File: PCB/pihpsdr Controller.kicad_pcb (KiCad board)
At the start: 2 copper layers, 243 x 154 mm, 167 parts, among them IC1 MCP23017T-E_SO, IC2 MCP23017T-E_SO, IC3 M24C32-RDW6TP, IC4 74LV1T125GVH, IC5 74LV1T125GVH, IC6 WM8960CGEFL_V, IC7 DS3231MZ_V+, IC8 Pico, J1 615008143721, J2 1725672, J3 485-1992, J4 SJ-3566AN, J5 SJ-3523-SMT-TR, J6 10129379-905001BLF, J7 Conn_01x02, J8 PJ-102AH, J9 MJ-3523-SMT, Q1 FDD6685, Q2 2N7002K, SW0 B3F-1055, SW1 B3F-1055, SW10 B3F-1055, SW11 B3F-1055, SW12 B3F-1055, SW13 B3F-1055, SW14 B3F-1055, SW15 B3F-1055, SW16 B3F-1055, SW2 B3F-1055, SW3 B3F-1055, SW4 B3F-1055, SW5 B3F-1055, SW6 B3F-1055, SW7 B3F-1055, SW8 B3F-1055, SW9 B3F-1055, U1 LMZ22005TZ_NOPB, U2 BAT-HLD-001, Y1 TSX-3225_24.0000MF18X-C

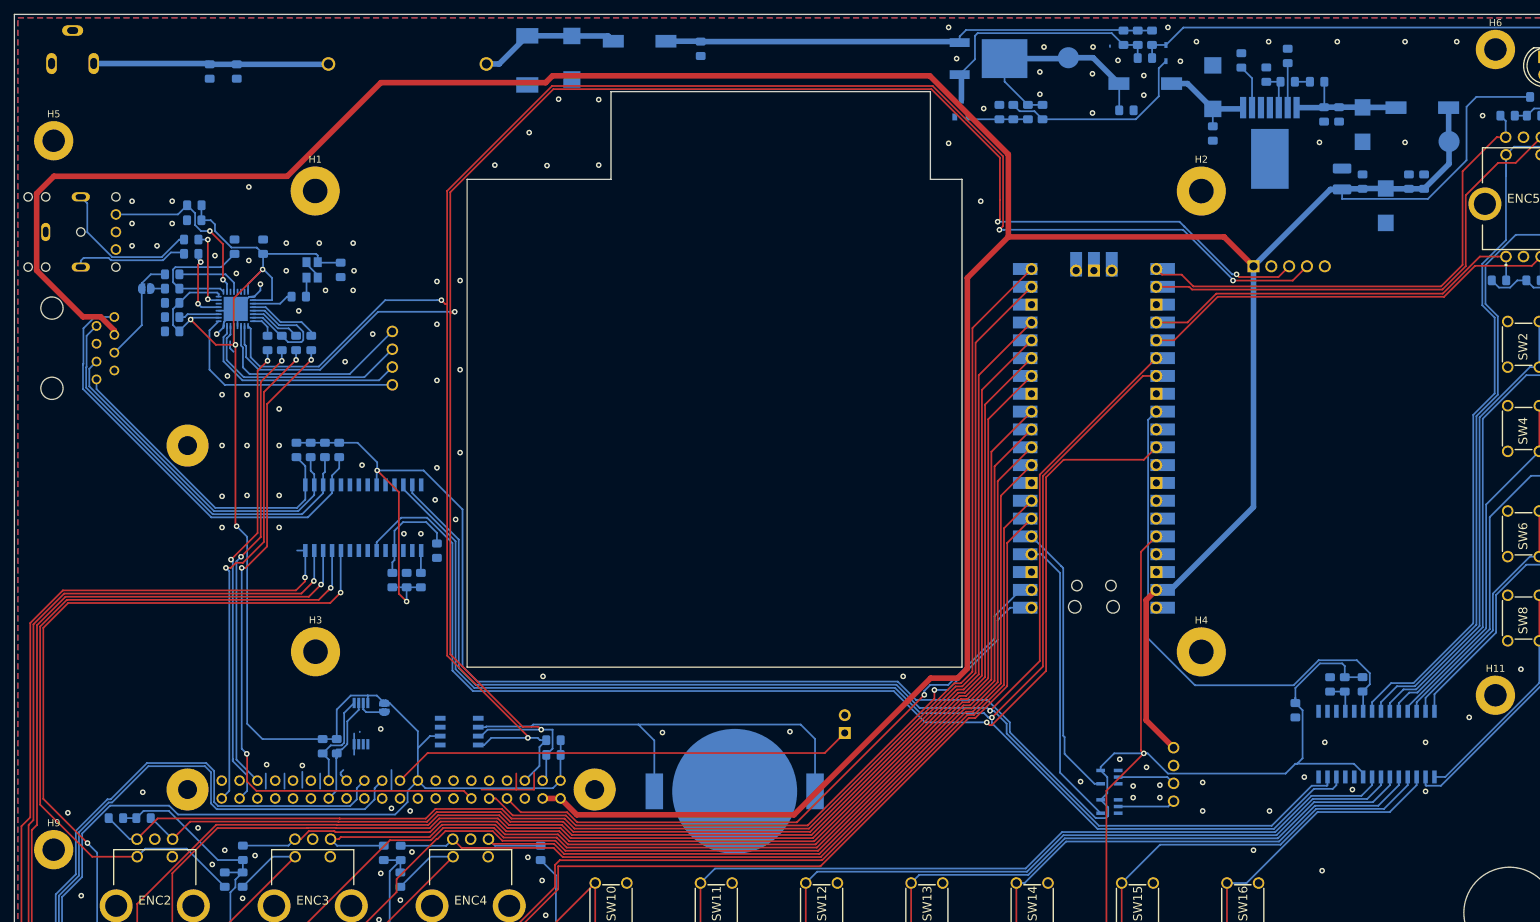
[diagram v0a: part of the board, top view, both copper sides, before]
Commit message: Completed parts details on schematics and recreated gerbers and bom.
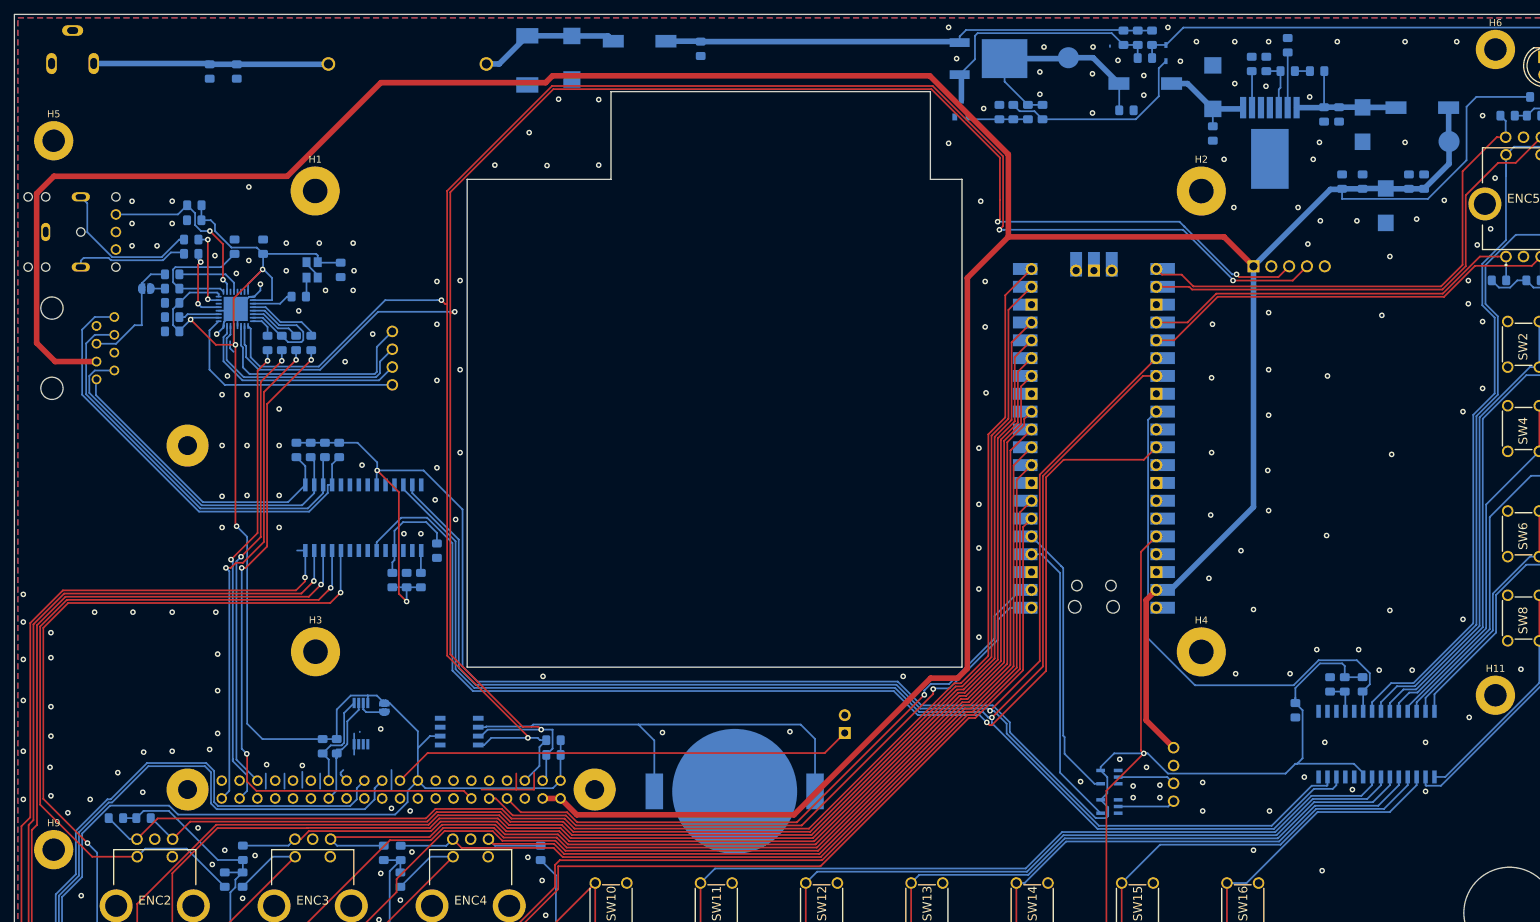
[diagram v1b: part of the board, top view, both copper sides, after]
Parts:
- C10, C11, C4, C9: value 4,7uF -> 4,7uF / 16V
- C12, C21, C23, C25: value 100nF 35V -> 0,1uF / 50V
- C13: value 0,1uF -> 0,1uF / 50V
- C14: value 10uF/35V -> 10uF / 35V
- C17: value 1uF / 10V -> 1uF / 50V
- C19: value 100nF -> 0,1uF / 50V
- C2: value 1µ -> 1uF / 50V
- C20, C24: value 10uF 35V -> 10uF / 35V
- C26: value 0,47nF -> 0,47uF / 16V
- C27, C30: value 100nF / 10V -> 0,1uF / 50V
- C33: value 10u -> 10u / 35V
- C34: value 100uF / 6.3V -> 100uF / 10V; footprint Capacitor_SMD:C_1210_3225Metric_Pad1.42x2.65mm_HandSolder -> Capacitor_SMD:C_0805_2012Metric_Pad1.15x1.40mm_HandSolder
- C5: value 0,1µF -> 0,1uF / 50V
- C6: value 0,1u -> 0,1uF / 50V
- C7, C8: value 100µF 10V -> 100uF / 10V
- moved R59 1.56 mm to (201.3, 22.1)
- moved C26 1.52 mm to (206.4, 19.4)
- moved R60 1.52 mm to (203.4, 22.1)
- moved R61 1.52 mm to (206.4, 23.1)
- moved R62 1.52 mm to (210.6, 23.1)
- moved C34 0.38 mm to (214.2, 38.8)
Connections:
- IC2 pad 1: MIC_FAST_SCAN -> MIC_BTN_DOWN
- IC2 pad 2: MIC_PTT -> MIC_BTN_UP
- IC2 pad 3: MIC_BTN_UP -> MIC_PTT
- IC2 pad 4: MIC_BTN_DOWN -> MIC_FAST_SCAN
- J1 pad 1: MIC_FAST_SCAN -> MIC_BTN_DOWN
- J1 pad 2: GND -> MIC_BTN_UP
- J1 pad 3: MIC_PTT -> +5V
- J1 pad 4: MIC+ -> GND
- J1 pad 5: GND -> MIC+
- J1 pad 6: +5V -> MIC_PTT
- J1 pad 7: MIC_BTN_UP -> GND
- J1 pad 8: MIC_BTN_DOWN -> MIC_FAST_SCAN
- R45 pad 2: MIC_FAST_SCAN -> MIC_BTN_DOWN
- R46 pad 2: MIC_PTT -> MIC_BTN_UP
- R47 pad 2: MIC_BTN_UP -> MIC_PTT
- R48 pad 2: MIC_BTN_DOWN -> MIC_FAST_SCAN
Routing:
- net MIC_BTN_DOWN: track 63.8 -> 43.9 mm
- net MIC_FAST_SCAN: track 45.2 -> 63.7 mm
- net MIC_PTT: track 49.9 -> 58.4 mm
- net MIC_BTN_UP: track 57.1 -> 51.0 mm
- net +5V: track 517.0 -> 521.7 mm
- net SPK_R-: track 30.2 -> 32.3 mm
- net MIC+: track 15.3 -> 17.3 mm
- net Net-(C27-Pad1): track 17.8 -> 19.4 mm
- net Net-(C26-Pad1): track 6.34 -> 7.86 mm
- net Net-(R60-Pad2): track 5.81 -> 7.34 mm
- net Net-(R59-Pad2): track 6.34 -> 5.22 mm
- net SPK_R+: track 31.3 -> 32.3 mm
- net GND: vias 136 -> 214

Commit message: Replaced RMS20 encoder with Chinese encoder. Maybe a modification of the encoder is necessary due to internal 7805 voltage regulator.
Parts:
- removed IC4, IC5: 74LV1T125GVH, SamacSys_Parts:SOT95P275X110-5N
- added R68: 10k, Resistor_SMD:R_0805_2012Metric_Pad1.15x1.40mm_HandSolder, B.Cu at (182.9, 123.8)
- added R69: 10k, Resistor_SMD:R_0805_2012Metric_Pad1.15x1.40mm_HandSolder, B.Cu at (182.9, 127.6)
- moved C15 6.78 mm to (208.2, 105.1)
- moved IC1 6.78 mm to (214.9, 113.6)
- moved R15 6.78 mm to (210.3, 105.1)
- moved R3 6.78 mm to (212.9, 105.1)
- moved C1 6.78 mm to (203.3, 108.8)
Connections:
- ENC1 pad 3: Net-(ENC1-Pad3) -> ENC1+
- ENC1 pad 4: Net-(ENC1-Pad4) -> ENC1-
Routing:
- net +3V3: track 811.1 -> 738.8 mm, vias 4 -> 7
- net ENC1+: track 39.8 -> 49.8 mm
- net GND: track 47.1 -> 55.8 mm, vias 214 -> 248
- net Net-(ENC1-Pad3): track 8.26 -> 0.00 mm
- net IC1_INT: track 75.3 -> 67.0 mm
- net ENC1-: track 41.8 -> 50.0 mm
- net Net-(ENC1-Pad4): track 8.21 -> 0.00 mm
- net SW8: track 52.0 -> 57.7 mm
- net SW11: track 111.8 -> 116.5 mm
- net SDA1: track 226.3 -> 230.6 mm
- net SW12: track 98.0 -> 101.8 mm
- net SW9: track 50.7 -> 54.4 mm
- net SCL1: track 228.0 -> 231.6 mm
- net IC2_INT: track 169.1 -> 166.0 mm
- net (no net): track 1.99 -> 5.13 mm
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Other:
- outline, holes or cut-outs redrawn

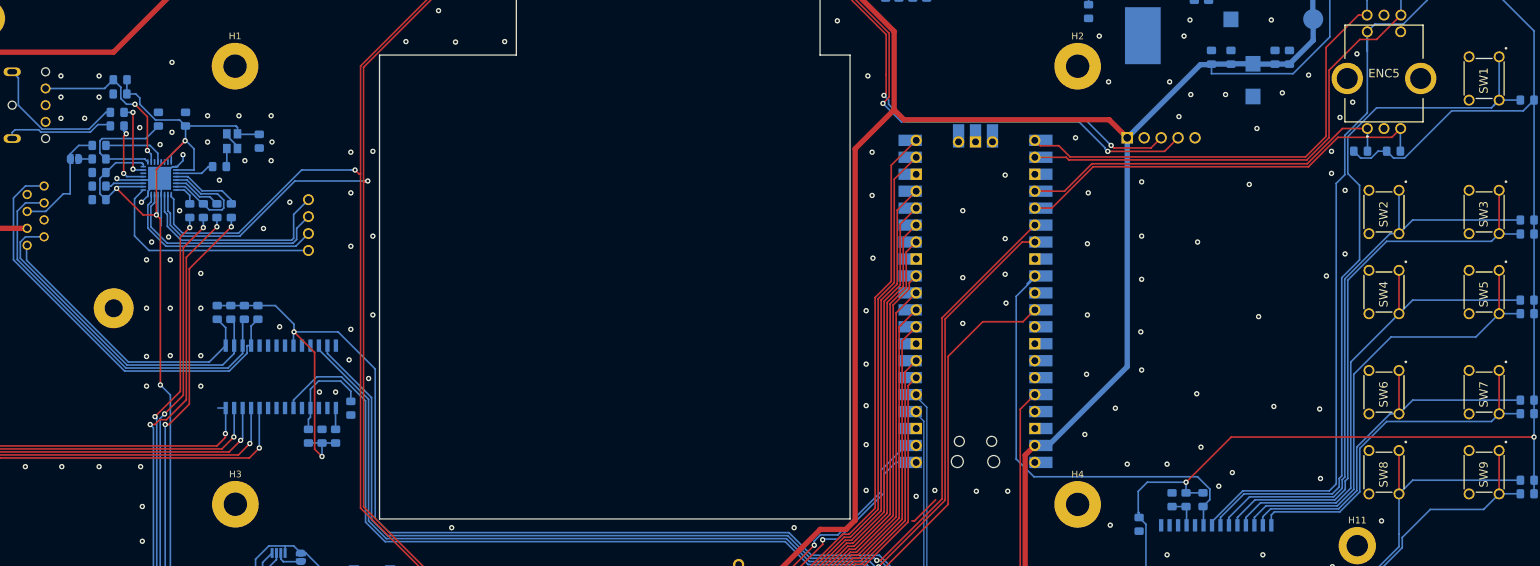
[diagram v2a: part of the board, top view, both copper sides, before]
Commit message: Refactored JLC Part Numbers. And replaced 100uF capacitors with 1206 sized parts.
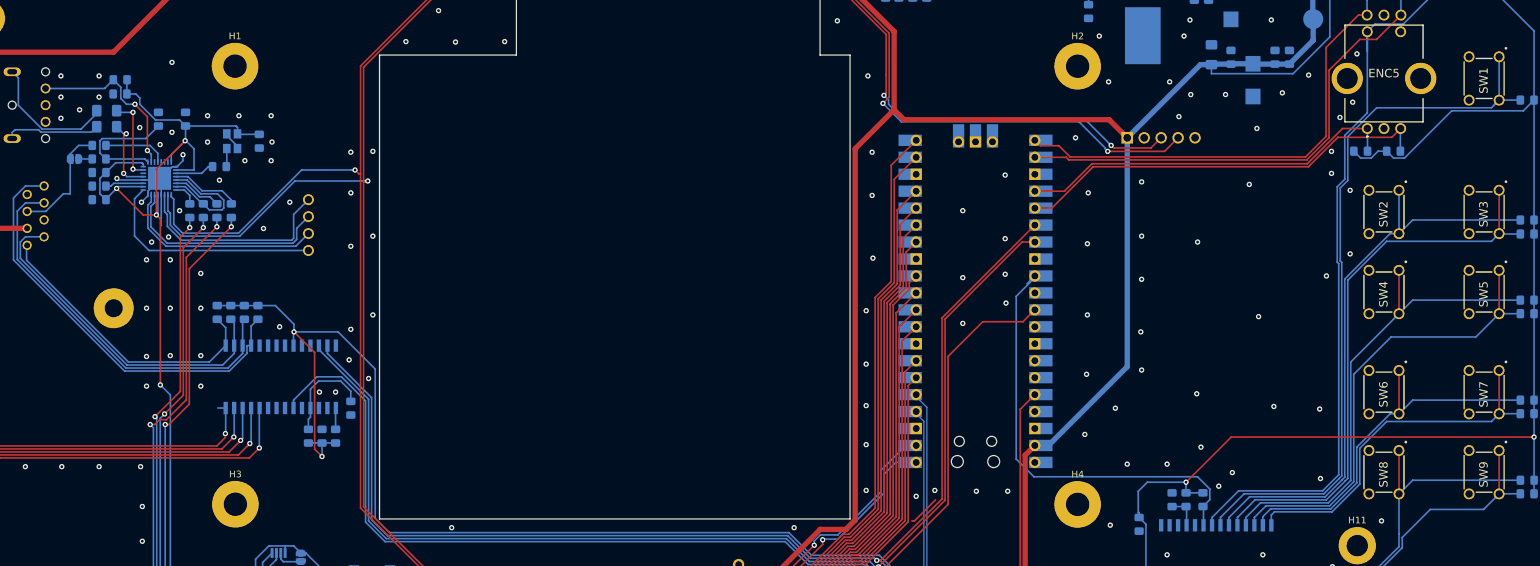
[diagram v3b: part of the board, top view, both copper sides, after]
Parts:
- C33: value 10u / 35V -> 10uF / 35V
- C34, C7, C8: footprint Capacitor_SMD:C_0805_2012Metric_Pad1.15x1.40mm_HandSolder -> Capacitor_SMD:C_1206_3216Metric_Pad1.42x1.75mm_HandSolder
- moved C7 1.59 mm to (48.6, 46.8)
- moved C8 1.58 mm to (48.6, 49.2)
- moved C34 0.38 mm to (214.2, 38.4)
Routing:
- net Net-(C8-Pad1): track 16.5 -> 14.2 mm
- net SW1: track 111.1 -> 109.1 mm
- net Net-(C7-Pad1): track 21.7 -> 20.0 mm
- net HP_L: track 11.6 -> 12.8 mm
- net SW3: track 85.8 -> 85.1 mm
- net SW2: track 87.9 -> 87.2 mm
- net SW7: track 55.5 -> 54.8 mm
- net SW4: track 73.4 -> 72.7 mm
- net SW6: track 57.4 -> 56.8 mm
- net SW5: track 70.3 -> 69.6 mm
- net HP_R: track 10.6 -> 11.1 mm

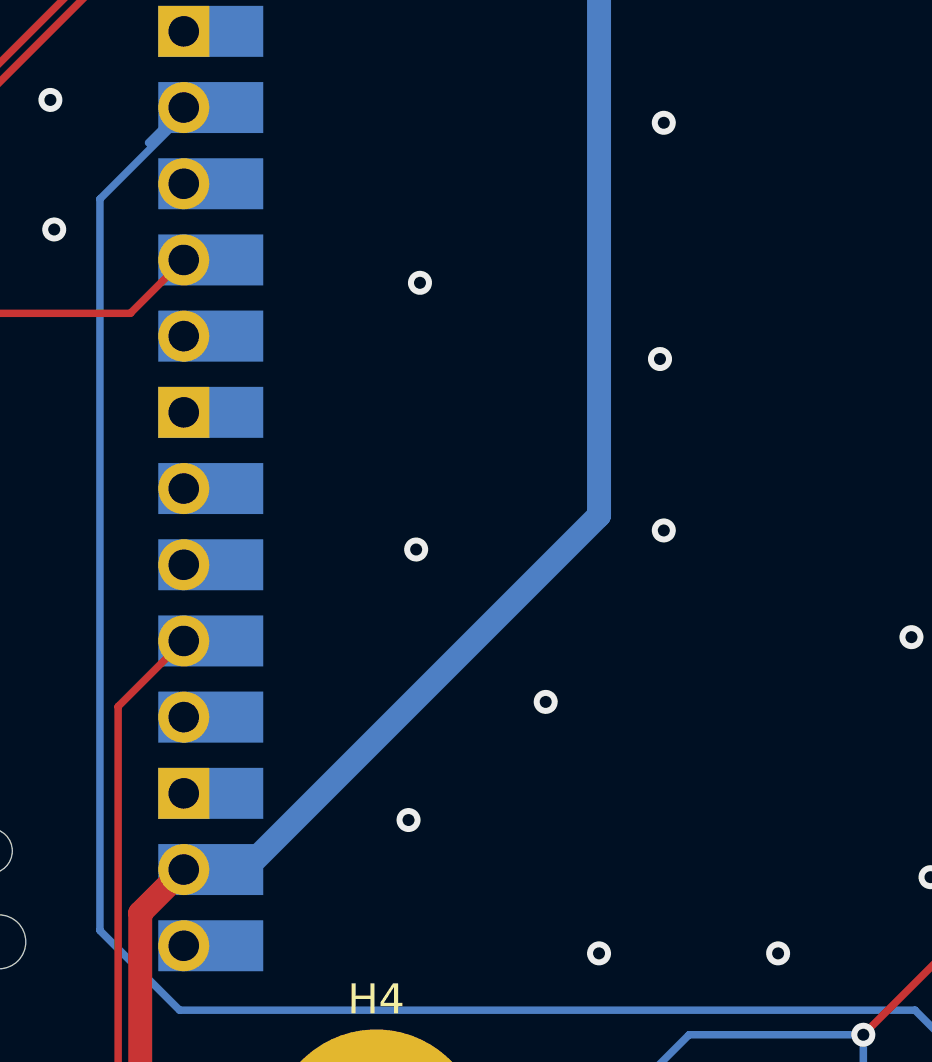
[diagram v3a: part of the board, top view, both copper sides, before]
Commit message: Added Reset Button to Pi Pico to make updating firmware easier.
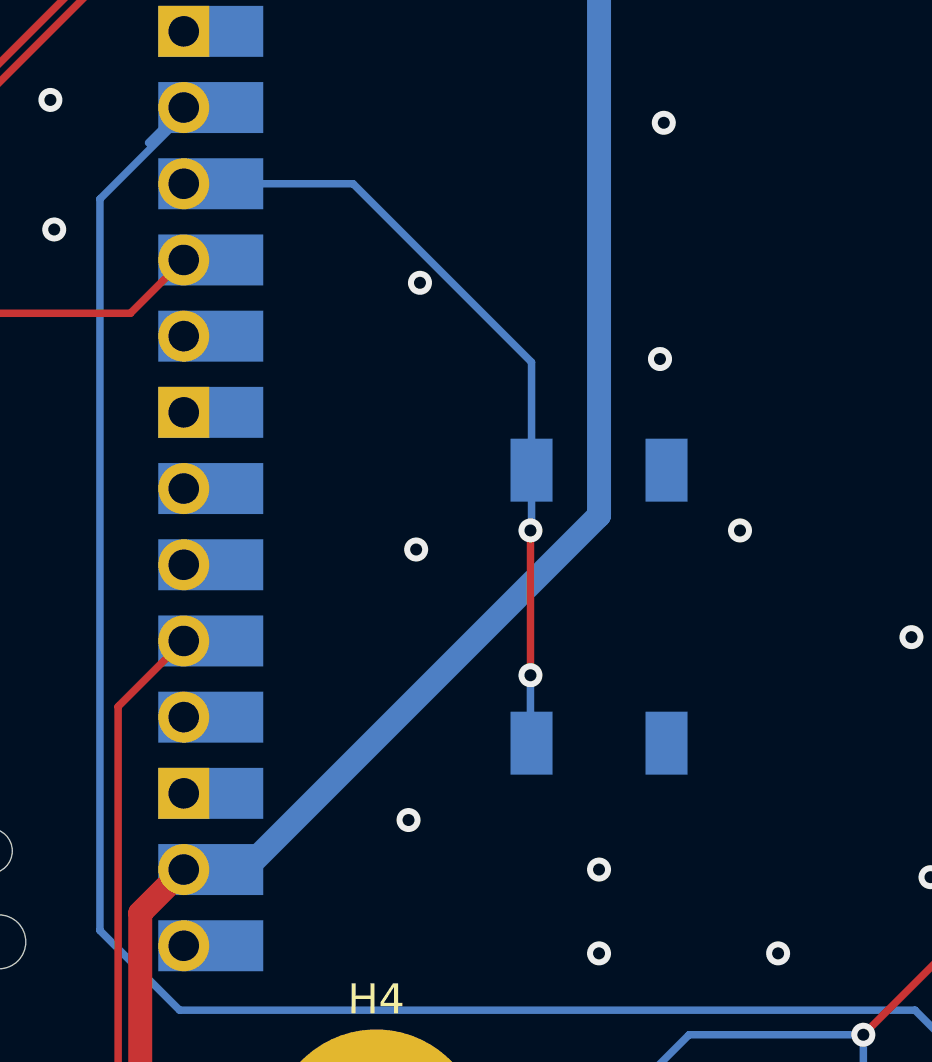
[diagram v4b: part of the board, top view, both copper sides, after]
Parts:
- added SW17: SW_SPST, SamacSys_Parts:TL3301SPF260QG, B.Cu at (201.5, 88.2)
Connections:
- IC8 pad 30: Net-(IC8-Pad30) -> /IC8_RESET
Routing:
- net /IC8_RESET: track 0.00 -> 26.8 mm, vias 0 -> 2
- net Net-(IC8-Pad30): vias 0 -> 1
- net GND: vias 248 -> 247

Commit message: Recreated some parts
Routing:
- net SW10: track 192.9 -> 191.7 mm
